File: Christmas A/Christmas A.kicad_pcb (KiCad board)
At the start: 2 copper layers, 80.1 x 97.8 mm, 21 parts, among them J1 LEFT, J2 RIGHT, J3 T_POS, J4 T_GND

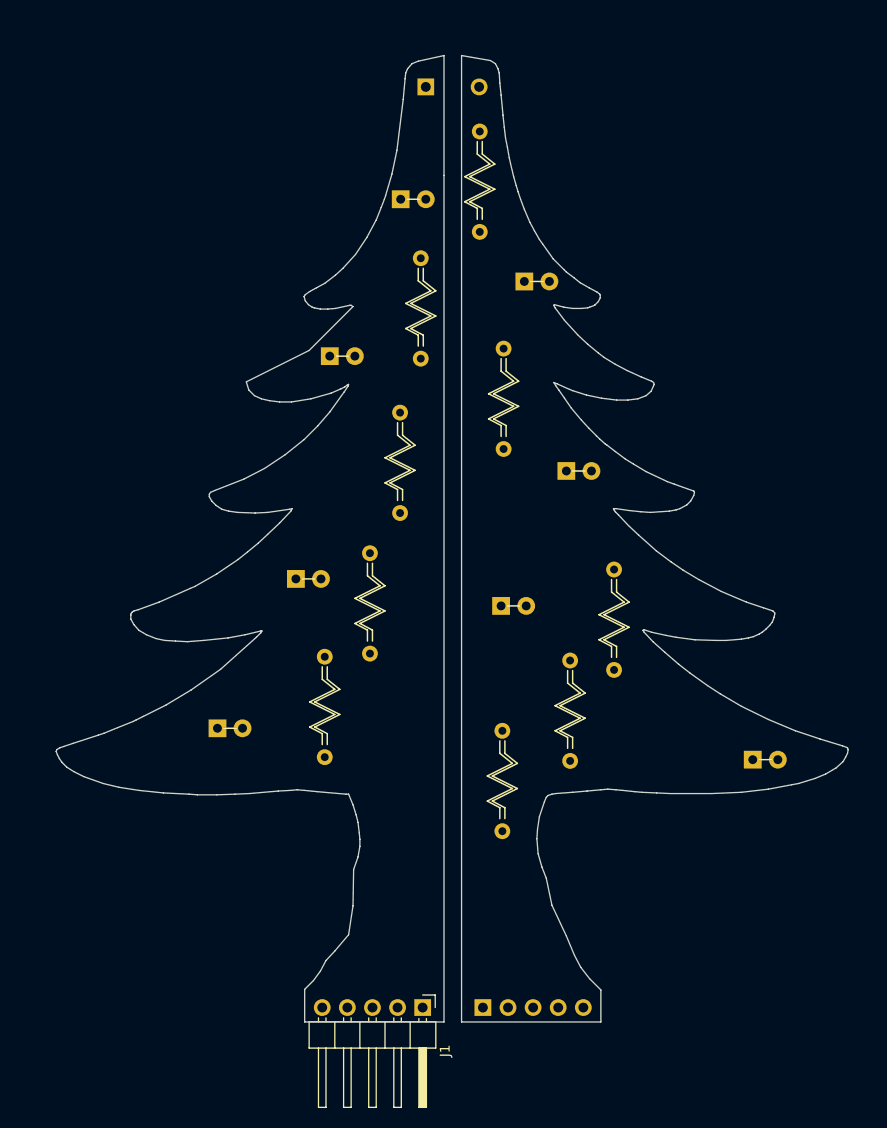
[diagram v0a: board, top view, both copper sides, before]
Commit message: Mirror components
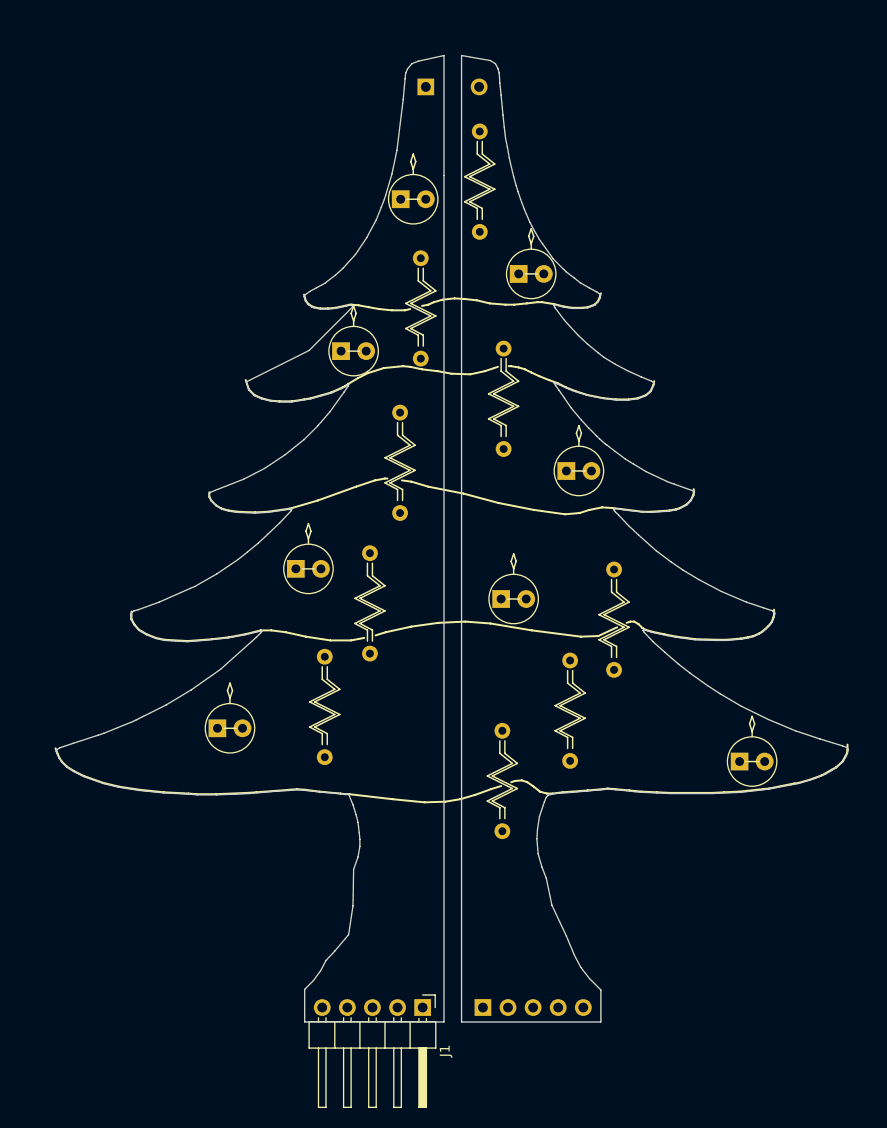
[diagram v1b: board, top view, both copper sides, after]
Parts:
- moved D9 1.35 mm to (133.8, 125.2)
- moved D3 1.25 mm to (93.5, 83.7)
- moved D4 1.02 mm to (88.9, 105.7)
- moved D6 0.95 mm to (111.4, 75.9)
- moved D8 0.70 mm to (109.7, 108.8)

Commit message: Stars added
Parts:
- added A?: STAR, christmas:star, B.Cu at (116.3, 83.6)
- added A?: STAR, christmas:star, B.Cu at (118.0, 103.4)
- added A?: STAR, christmas:star, F.Cu at (99.9, 119.3)
- added A?: STAR, christmas:star, B.Cu at (101.3, 121.3)
- added A?: STAR, christmas:star, B.Cu at (125.9, 122.9)
- added A?: STAR, christmas:star, F.Cu at (126.6, 120.6)
- added A?: STAR, christmas:star, F.Cu at (91.4, 94.7)

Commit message: Changed the top
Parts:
- removed the A? at (116.3, 83.6)
- removed the A? at (118.0, 103.4)
- removed the A? at (99.9, 119.3)
- removed the A? at (101.3, 121.3)
- removed the A? at (125.9, 122.9)
- removed the A? at (126.6, 120.6)
- removed the A? at (91.4, 94.7)
- removed J3: T_POS, christmas:t_pos
- removed J4: T_GND, christmas:t_gnd
- added A?: STAR, christmas:star, F.Cu at (99.5, 106.9)
- added A?: STAR, christmas:star, F.Cu at (95.8, 75.4)
- added A?: STAR, christmas:star, F.Cu at (126.7, 120.6)
- added A?: STAR, christmas:star, F.Cu at (115.4, 105.1)
- added A?: STAR, christmas:star, F.Cu at (98.3, 122.9)
- added A?: STAR, christmas:star, F.Cu at (92.6, 94.4)
- added A?: STAR, christmas:star, B.Cu at (98.9, 74.7)
- added A?: STAR, christmas:star, B.Cu at (126.3, 121.7)
- added A?: STAR, christmas:star, B.Cu at (100.0, 120.9)
- added A?: STAR, christmas:star, B.Cu at (94.6, 93.2)
- added A?: STAR, christmas:star, B.Cu at (129.8, 109.5)
- added A?: STAR, christmas:star, B.Cu at (109.7, 102.2)
- added A?: STAR, christmas:star, B.Cu at (115.5, 83.3)
- added A?: STAR, christmas:star, F.Cu at (114.7, 84.3)
- added D1: LED_Small, christmas:top_star, F.Cu at (103.4, 53.9)
- moved R1 1.40 mm to (107.5, 60.1)
- moved D2 1.16 mm to (99.7, 67.2)
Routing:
- net Net-(J1-Pad1): track 0.00 -> 82.3 mm
- net Net-(J1-Pad2): track 0.00 -> 68.2 mm
- net Net-(J2-Pad1): track 0.00 -> 59.1 mm, vias 0 -> 1
- net Net-(J1-Pad3): track 0.00 -> 56.0 mm
- net Net-(J2-Pad2): track 0.00 -> 47.8 mm, vias 0 -> 1
- net Net-(J1-Pad4): track 0.00 -> 44.7 mm, vias 0 -> 1
- net Net-(J1-Pad5): track 0.00 -> 39.1 mm, vias 0 -> 1
- net Net-(J2-Pad3): track 0.00 -> 35.2 mm, vias 0 -> 1
- net Net-(D9-Pad2): track 0.00 -> 30.2 mm
- net Net-(J2-Pad4): track 0.00 -> 20.7 mm
- net Net-(D5-Pad2): track 0.00 -> 15.2 mm, vias 0 -> 1
- net Net-(D7-Pad2): track 0.00 -> 10.9 mm
- net Net-(D8-Pad2): track 0.00 -> 10.1 mm
- net Net-(D6-Pad2): track 0.00 -> 9.24 mm
- net Net-(D3-Pad2): track 0.00 -> 8.76 mm
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- added copper zone on F.Cu, net /GND
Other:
- board size 80.1 x 97.8 mm -> 80.1 x 99.5 mm

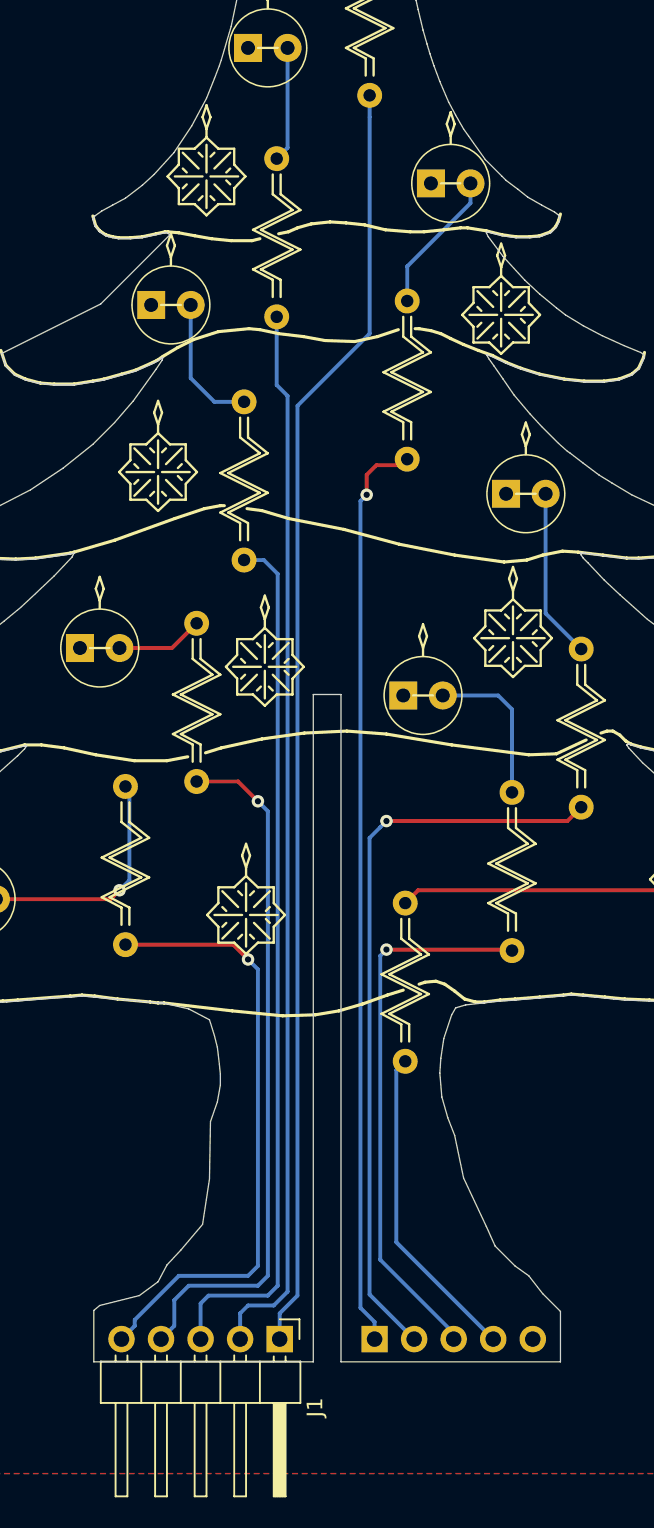
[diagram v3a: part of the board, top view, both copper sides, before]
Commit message: Make space at the bottom
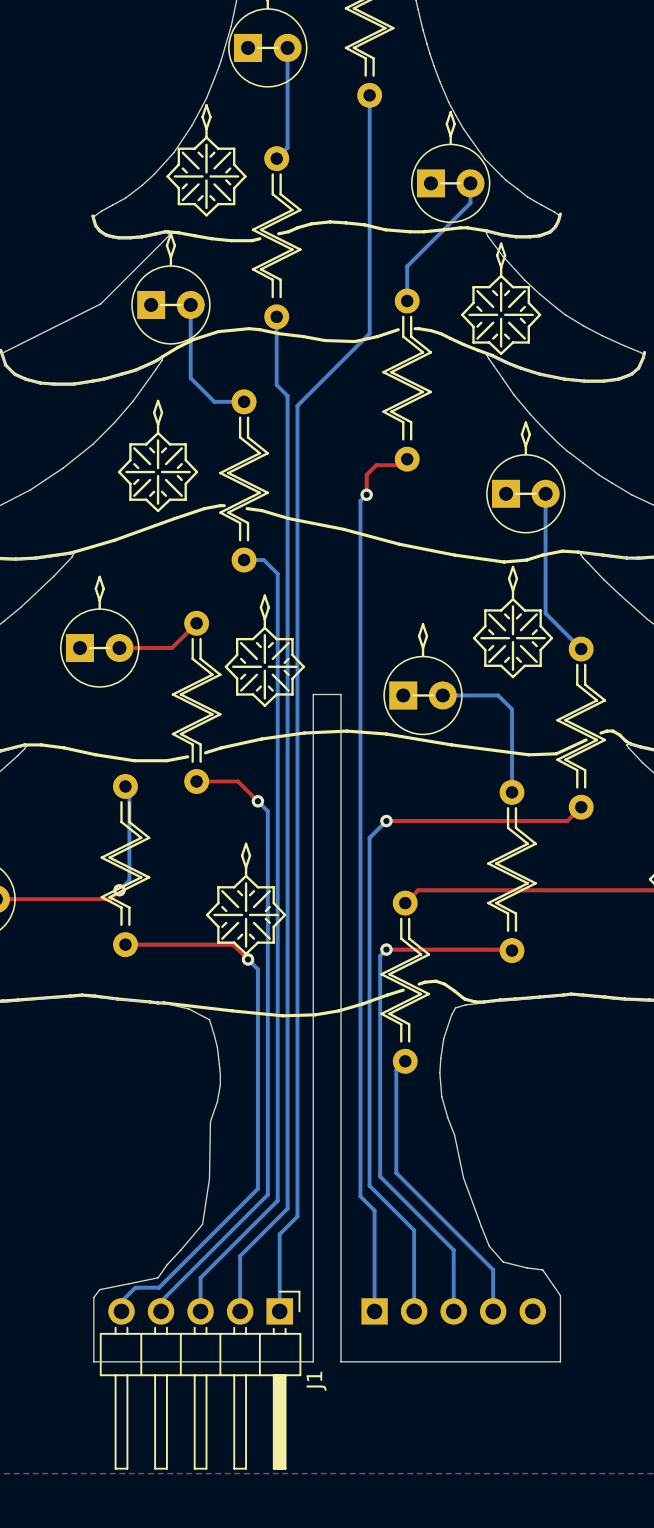
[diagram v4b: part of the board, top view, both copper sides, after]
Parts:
- moved J1 1.78 mm to (101.7, 148.3)
- moved J2 1.78 mm to (107.8, 148.3)
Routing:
- net Net-(J1-Pad4): track 44.7 -> 40.3 mm
- net Net-(J1-Pad3): track 56.0 -> 51.9 mm
- net Net-(J1-Pad5): track 39.1 -> 35.7 mm
- net Net-(J1-Pad2): track 68.2 -> 65.4 mm
- net Net-(J2-Pad4): track 20.7 -> 18.9 mm
- net Net-(J2-Pad3): track 35.2 -> 33.5 mm
- net Net-(J2-Pad2): track 47.8 -> 46.0 mm
- net Net-(J2-Pad1): track 59.1 -> 57.3 mm
- net Net-(J1-Pad1): track 82.3 -> 80.5 mm
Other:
- outline, holes or cut-outs redrawn

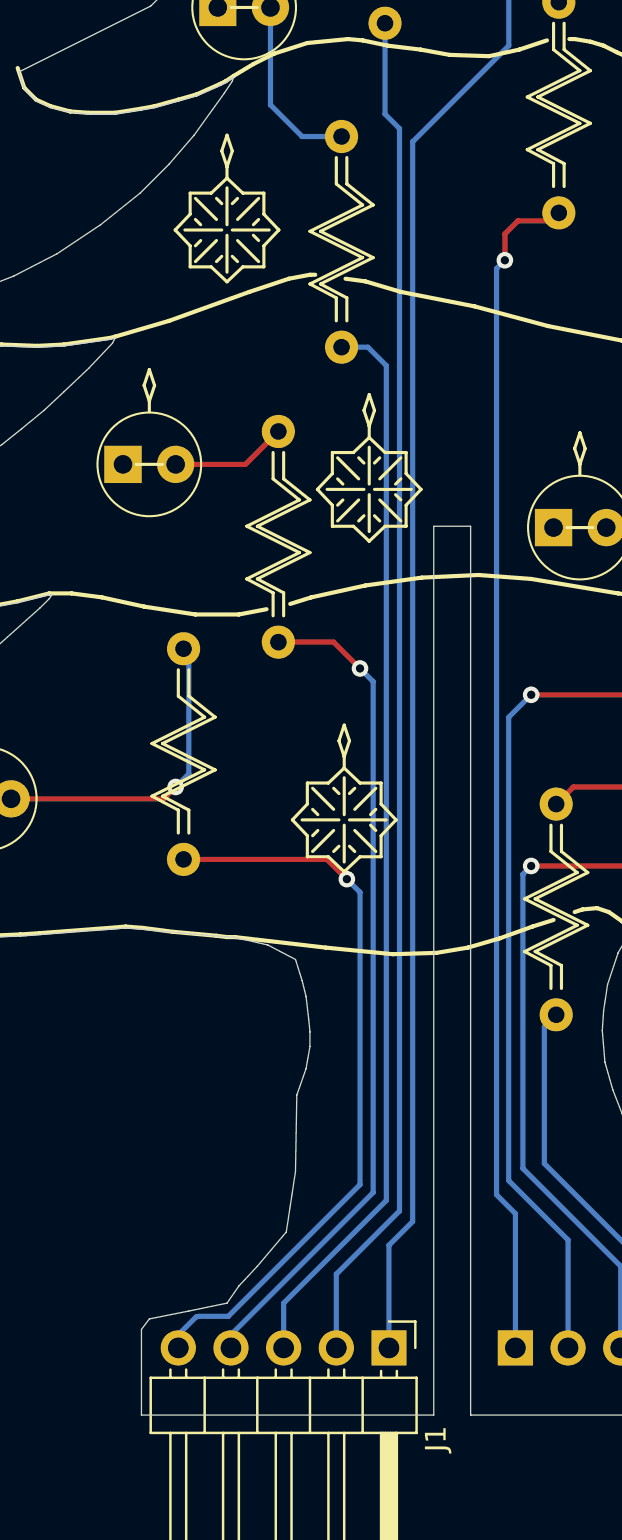
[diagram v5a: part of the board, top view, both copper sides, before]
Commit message: Added markings to part A
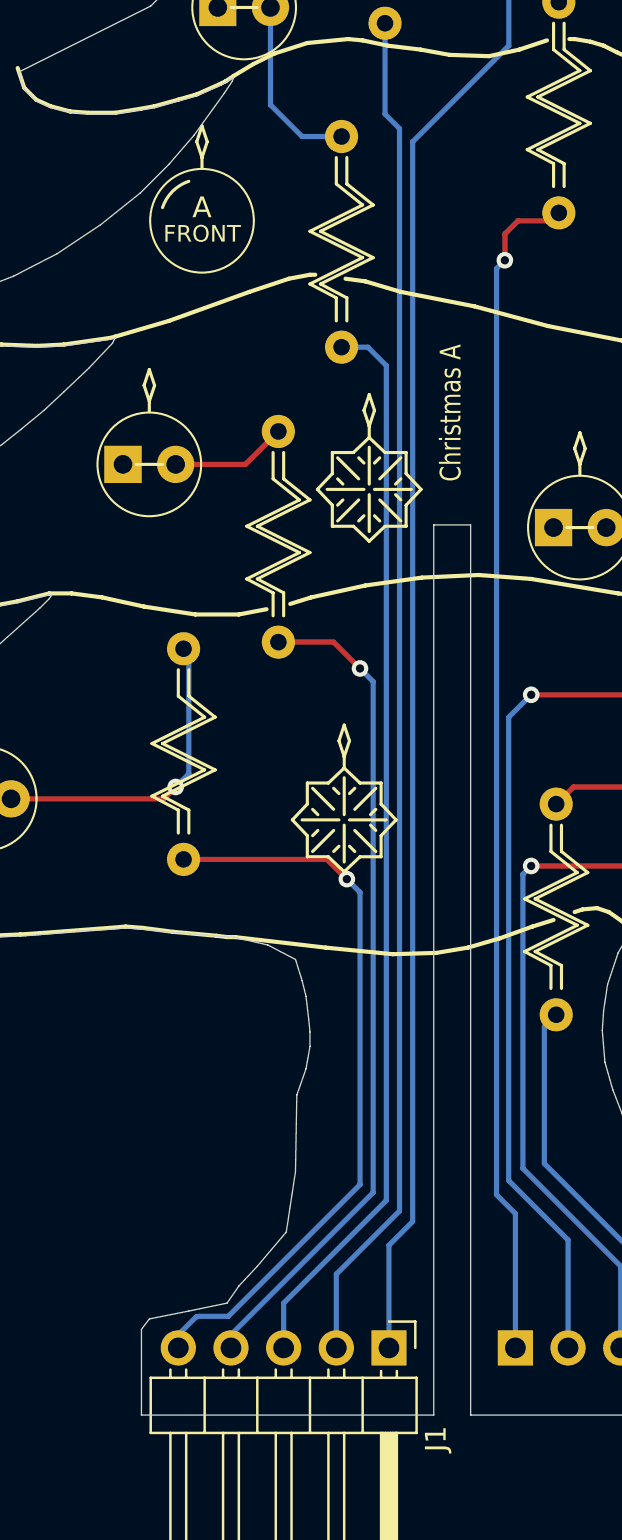
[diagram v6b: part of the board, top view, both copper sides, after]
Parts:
- removed the A? at (92.6, 94.4)
- removed the A? at (94.6, 93.2)
- added A?: Part A, christmas:part_a, F.Cu at (91.4, 94.0)
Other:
- board text added: "Christmas A"
- board text added: "github.com/tebl"
